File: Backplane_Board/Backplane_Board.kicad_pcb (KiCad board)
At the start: 4 copper layers, 179.7 x 127.9 mm, 175 parts, among them J1 XT60, J10 Conn_01x02_Pin, J11 Conn_01x02_Pin, J12 Conn_01x02_Pin, J13 Conn_01x02_Pin, J14 Conn_01x02_Pin, J15 Conn_01x02_Pin, J16 Conn_01x02_Pin, J17 Conn_01x02_Pin, J18 Conn_01x02_Pin, J19 Conn_01x02_Pin, J2 XT60, J20 Conn_01x02_Pin, J21 Conn_01x02_Pin, J22 Conn_01x02_Pin, J23 Conn_01x02_Pin, J24 Conn_01x02_Pin, J25 Conn_01x02_Pin, J26 Conn_01x02_Pin, J27 Conn_01x03_Pin, J28 Conn_01x03_Pin, J29 Conn_01x03_Pin, J3 Conn_01x02_Pin, J30 BM03B-SRSS-TB, J31 Conn_01x04, J32 Conn_01x05_Socket, J33 BM03B-SRSS-TB, J34 Connector_PinHeader_2.54mm:Pi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, J35 Connector_PinHeader_2.54mm:Pi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, J36 Conn_01x03_Pin, J37 Conn_01x02, J38 Conn_01x02, J39 Conn_01x02, J4 Conn_01x07_Female, J40 Conn_01x02, J41 Conn_01x02, J42 Conn_01x02, J5 Conn_01x02_Pin, J6 Conn_01x02_Pin, J7 Conn_01x02_Pin, J8 Conn_01x02_Pin, J9 Conn_01x02_Pin, Q1 FDMS86163P, Q2 FDMS86163P, Q3 SI7615ADN-T1-GE3, Q4 ZXMN3A14F, Q5 ZXMN3A14F, Q6 ZXMN3A14F, Q7 ZXMN3A14F, Q8 ZXMN3A14F, Q9 ZXMN3A14F, SW1 SW_DPST_x2, U1 ZXTR2005ZQ-13, U2 PINA740AIREMR, U3 PKJ7213WPI, U4 PKJ7213WPI, U5 PKU3511SPI, U6 Pico

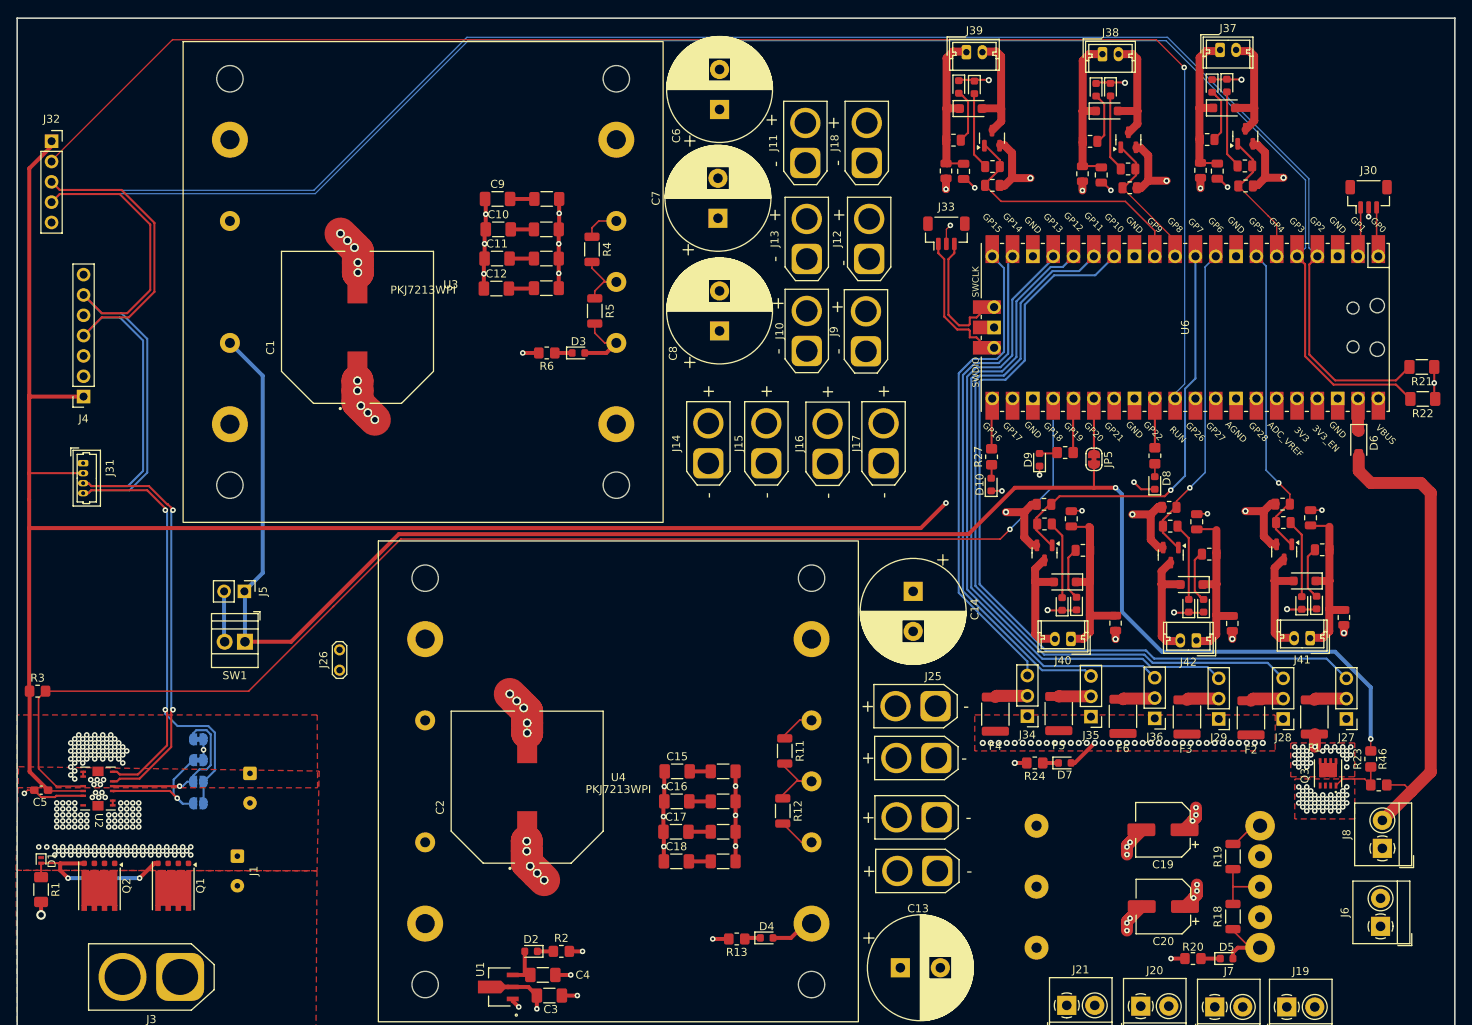
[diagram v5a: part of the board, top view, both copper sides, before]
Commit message: added sd card, more drc stuff to fix
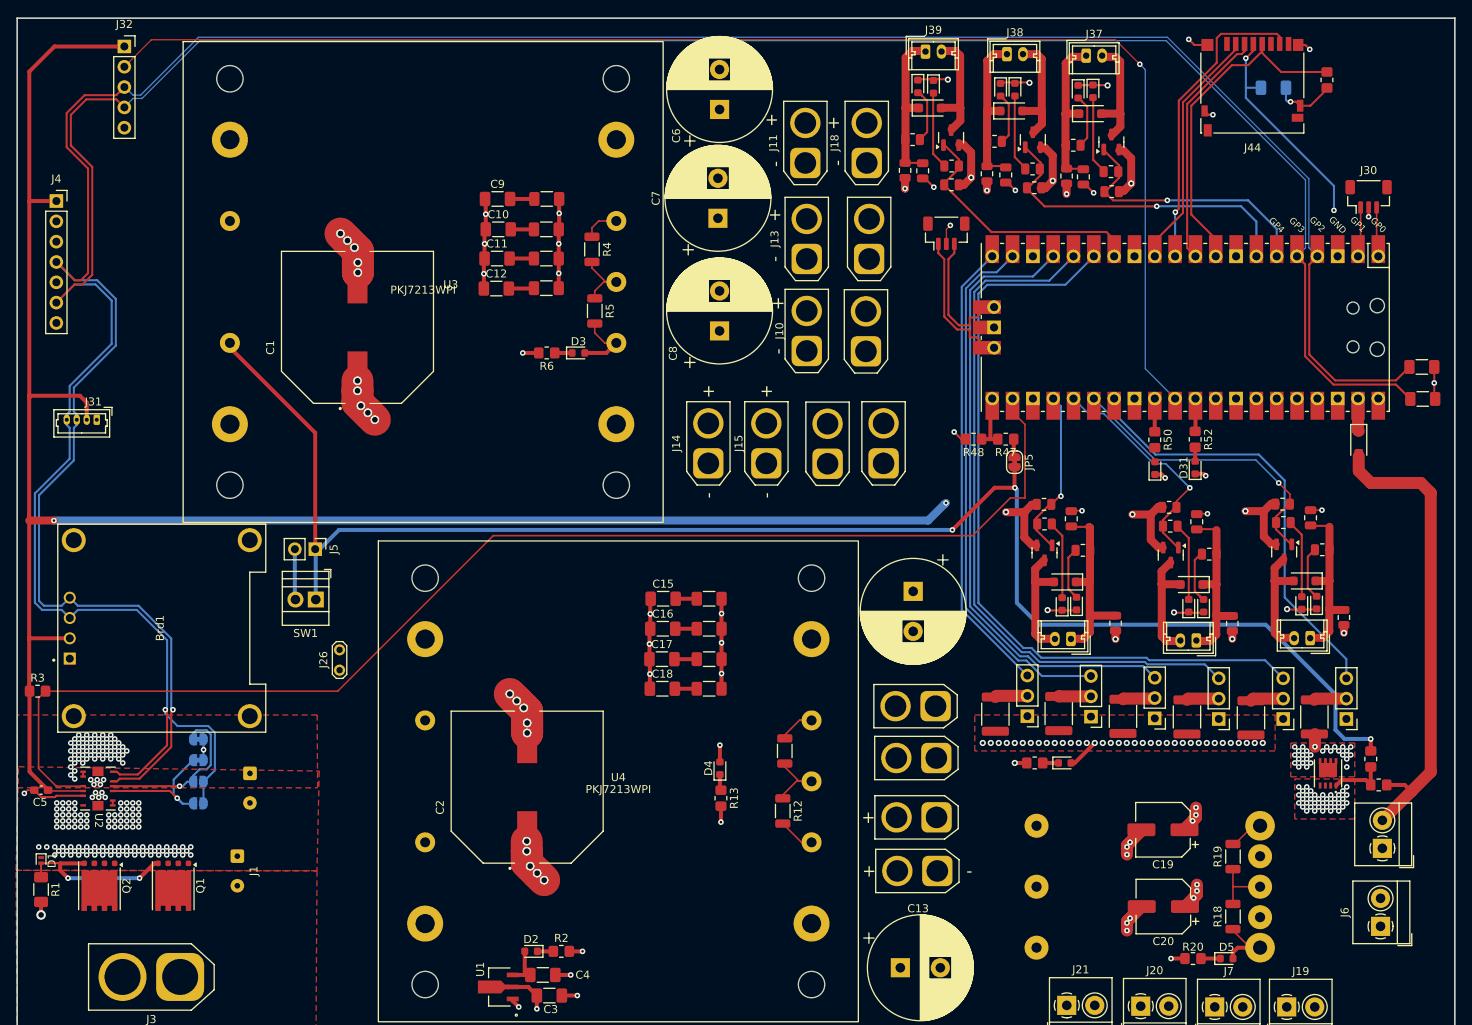
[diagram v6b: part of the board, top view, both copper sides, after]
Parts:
- removed D10, D8, D9: LED, LED_SMD:LED_0603_1608Metric
- removed R25, R26, R27: 1K, Resistor_SMD:R_0805_2012Metric_Pad1.20x1.40mm_HandSolder
- added Brd1: SSD1306, SSD1306IW:MODULE_DM-OLED096-636, F.Cu at (49.4, 99.7)
- added C27: C, Capacitor_SMD:C_1206_3216Metric_Pad1.33x1.80mm_HandSolder, B.Cu at (188.3, 32.1)
- added D30: LED, LED_SMD:LED_0603_1608Metric, F.Cu at (173.5, 79.7)
- added D31: LED, LED_SMD:LED_0603_1608Metric, F.Cu at (178.6, 79.6)
- added J44: Micro_SD_Card_Det2, Connector_Card:microSD_HC_Hirose_DM3D-SF, F.Cu at (185.7, 32.0)
- added R47: 10K, Resistor_SMD:R_0805_2012Metric_Pad1.20x1.40mm_HandSolder, F.Cu at (154.9, 76.0)
- added R48: 20K, Resistor_SMD:R_0805_2012Metric_Pad1.20x1.40mm_HandSolder, F.Cu at (150.8, 76.0)
- added R50: 1K, Resistor_SMD:R_0805_2012Metric_Pad1.20x1.40mm_HandSolder, F.Cu at (173.5, 76.1)
- added R51: DNP, Resistor_SMD:R_0805_2012Metric_Pad1.20x1.40mm_HandSolder, F.Cu at (195.0, 31.1)
- added R52: 1K, Resistor_SMD:R_0805_2012Metric_Pad1.20x1.40mm_HandSolder, F.Cu at (178.6, 76.0)
- moved J4 24.7 mm to (36.2, 46.3), turned to 0 degrees
- moved D4 22.0 mm to (119.1, 117.2), turned to 90 degrees
- moved C18 21.6 mm to (112.0, 107.2)
- moved C15 21.6 mm to (112.0, 96.0)
- moved C16 21.6 mm to (112.0, 99.7)
- moved R14 21.6 mm to (117.9, 95.9)
- moved R15 21.6 mm to (117.9, 99.6)
- moved R16 21.6 mm to (117.9, 103.4)
- moved C17 21.6 mm to (111.9, 103.5)
- moved R17 21.6 mm to (117.9, 107.1)
- moved R13 17.7 mm to (119.3, 120.9), turned to -90 degrees
- moved D11 16.8 mm to (163.9, 32.6)
- moved D14 16.8 mm to (165.4, 35.3)
- moved D17 16.8 mm to (165.8, 32.5)
- moved F7 16.8 mm to (162.5, 43.1)
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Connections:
- JP5 pad 1: esc_status -> Net-(JP5-A)
- U6 pad 10: SW5 -> MOSI
- U6 pad 11: SW0 -> MISO
- U6 pad 12: SW1 -> CS
- U6 pad 14: SERVO0 -> SW1
- U6 pad 21: Net-(U6-GPIO16) -> esc_status
- U6 pad 22: unconnected-(U6-GPIO17-Pad22)_1 -> ALERT
- U6 pad 24: ALERT -> SW5
- U6 pad 25: Net-(U6-GPIO19) -> SW4
- U6 pad 26: esc_status -> SW3
- U6 pad 27: unconnected-(U6-GPIO21-Pad27)_1 -> SERVO0
- U6 pad 31: unconnected-(U6-GPIO26_ADC0-Pad31) -> Net-(U6-GPIO26_ADC0)
- U6 pad 7: SW3 -> SW0
- U6 pad 9: SW4 -> SCK
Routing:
- net +3.3V: track 221.3 -> 274.8 mm, vias 2 -> 5
- net SERVO0: track 103.4 -> 54.6 mm
- net SCK: track 0.00 -> 42.9 mm
- net MISO: track 0.00 -> 38.6 mm, vias 0 -> 1
- net SW5: track 52.8 -> 20.9 mm
- net CS: track 0.00 -> 30.7 mm
- net MOSI: track 0.00 -> 30.3 mm
- net KillSW: track 219.6 -> 199.6 mm, vias 2 -> 3
- net SW0: track 22.1 -> 41.4 mm, vias 0 -> 1
- net RUN: track 191.3 -> 173.2 mm
- net SW2: track 17.4 -> 33.6 mm, vias 0 -> 1
- net SW4: track 40.1 -> 28.9 mm
- net I2C+: track 333.5 -> 324.7 mm, vias 2 -> 1
- net Net-(U6-GPIO19): track 6.87 -> 0.00 mm
- net Net-(U6-GPIO16): track 6.31 -> 0.00 mm
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
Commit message: clean up
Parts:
- removed J1, J2: XT60, Connector_Wire:SolderWire-0.127sqmm_1x02_P3.7mm_D0.48mm_OD1mm
- added H1: MountingHole_Pad, MountingHole:MountingHole_4.3mm_M4_Pad_Via, F.Cu at (204.2, 145.0)
- added H2: MountingHole_Pad, MountingHole:MountingHole_4.3mm_M4_Pad_Via, F.Cu at (202.3, 31.7)
- added H3: MountingHole_Pad, MountingHole:MountingHole_4.3mm_M4_Pad_Via, F.Cu at (38.3, 144.3)
- added H4: MountingHole_Pad, MountingHole:MountingHole_4.3mm_M4_Pad_Via, F.Cu at (37.7, 29.3)
- added TP1: TestPoint, TestPoint:TestPoint_Loop_D1.80mm_Drill1.0mm_Beaded, F.Cu at (47.0, 64.0)
- added TP2: TestPoint, TestPoint:TestPoint_Loop_D1.80mm_Drill1.0mm_Beaded, F.Cu at (40.0, 64.0)
- added TP3: TestPoint, TestPoint:TestPoint_Pad_2.5x2.5mm, B.Cu at (206.0, 57.0)
- added TP4: TestPoint, TestPoint:TestPoint_Pad_2.5x2.5mm, B.Cu at (195.0, 57.0)
- added TP5: TestPoint, TestPoint:TestPoint_Pad_2.5x2.5mm, B.Cu at (42.0, 134.2)
- added TP6: TestPoint, TestPoint:TestPoint_Pad_2.5x2.5mm, B.Cu at (72.2, 91.1)
- added TP7: TestPoint, TestPoint:TestPoint_Pad_2.5x2.5mm, B.Cu at (147.6, 80.5)
- moved J3 8.77 mm to (60.0, 146.0)
- moved J30 4.57 mm to (204.8, 45.7), turned to -90 degrees
- moved J6 0.78 mm to (202.0, 136.2)
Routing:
- net UART(RX): track 6.25 -> 17.0 mm
- net UART(TX): track 6.20 -> 14.4 mm
- net GND: track 188.4 -> 195.0 mm
- net KillSW: track 199.6 -> 203.5 mm
- net Net-(D1-A): track 21.4 -> 24.7 mm
- net Net-(D30-A): track 0.00 -> 1.77 mm
- net +3.3V: track 274.8 -> 273.2 mm
- net I2C+: track 324.7 -> 324.0 mm
- net I2C-: track 340.4 -> 340.9 mm
- net 60V: vias 70 -> 217
